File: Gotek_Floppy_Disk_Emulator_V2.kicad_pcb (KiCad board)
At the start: 2 copper layers, 90 x 60 mm, 66 parts, among them J1 Power Connector, J2 OLED Display 0.91" Module, J3 USB_A, J5 Programming Connector, J6 Floppy Data Connector, Q1 MMBT2222, Q2 BSS123, Q3 BSS123, Q4 BSS123, Q5 BSS123, Q6 BSS123, Q7 BSS123, SW1 KY040 Rotary Encoder Module, SW2 DIP Switch, U1 AMS1117-3.3, U2 STM32F105RBTx, U3 STMPS2141, U4 74HCT04, Y1 8MHz

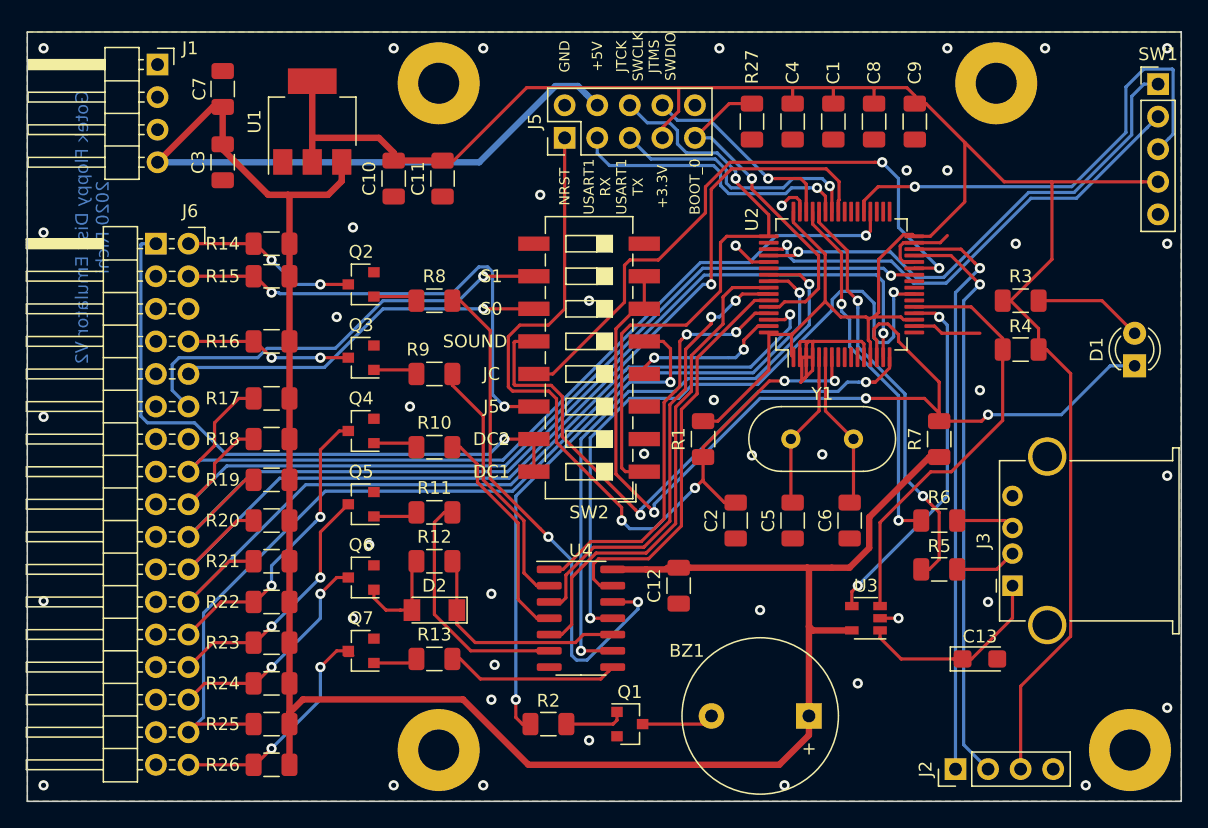
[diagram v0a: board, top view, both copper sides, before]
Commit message: Fixed PCB from original https://github.com/RichardRozehnal/Gotek-Floppy-Disk-Emulator-V2: * Add PCB edge cut for IDC 34-pin cable keying * Change Buzzer type from Active to Passive (single click on drive motor step) * Change "Buzzer_12x9.5RM7.6" footprint to "Buzzer_12x9.5RM6.5"
Update BoM.
Add Buzzer_12x9.5RM6.5 footprint and 3D model.
Delete unused files.
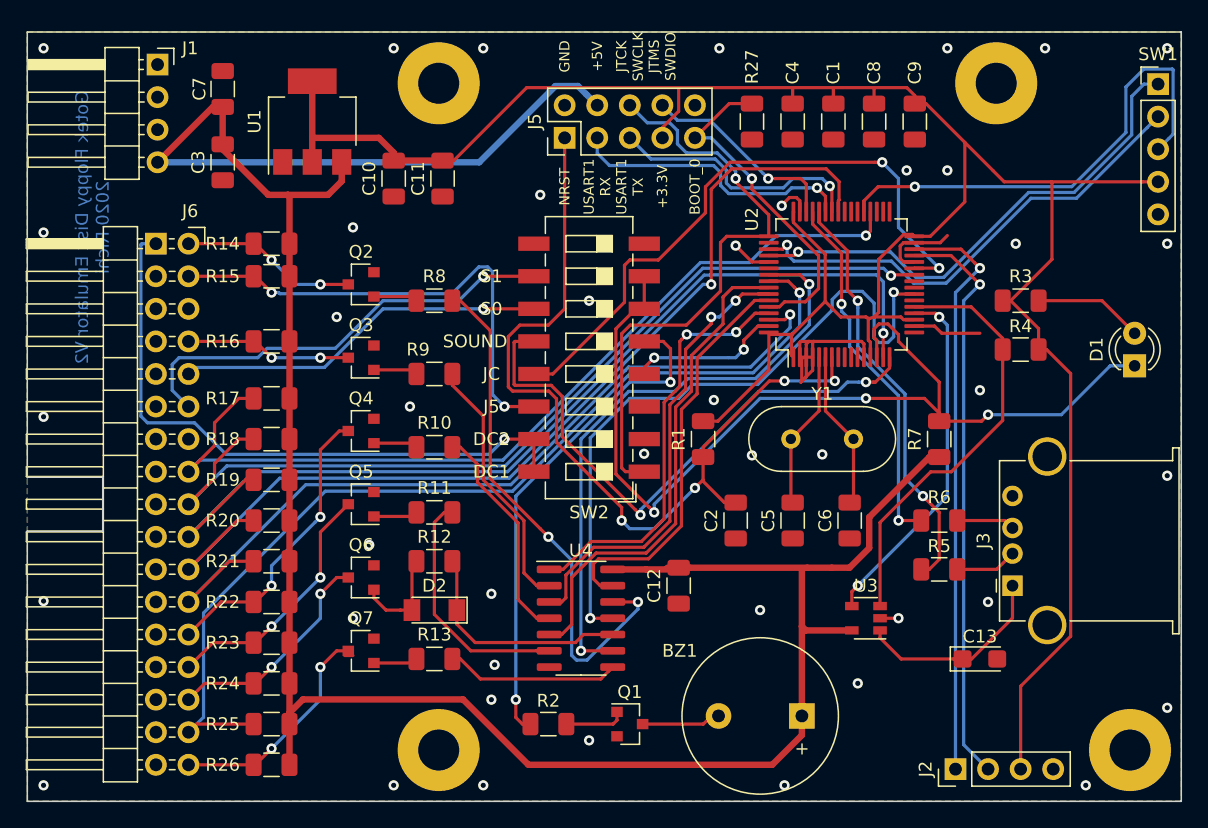
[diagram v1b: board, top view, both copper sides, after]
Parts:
- BZ1: value 5V Active Buzzer 12mm -> 5V Passive Buzzer 12mm; footprint Gotek_Floppy_Disk_Emulator_V2:Buzzer_12x9.5RM7.6 -> Gotek_Floppy_Disk_Emulator_V2:Buzzer_12x9.5RM6.5
- moved BZ1 0.55 mm to (142.3, 109.2)
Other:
- outline, holes or cut-outs redrawn
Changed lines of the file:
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@@
   (general
     (thickness 1.6)
-    (drawings 23)
-    (tracks 855)
+    (drawings 27)
+    (tracks 854)
     (zones 0)
     (modules 66)
@@
     (add_net +5V)
   )
+  (module Gotek_Floppy_Disk_Emulator_V2:Buzzer_12x9.5RM6.5 (layer F.Cu)
+    (at 142.325 109.22 180)
+    (descr "Generic Buzzer, D12mm height 9.5mm with RM6.5mm")
+    (tags buzzer)
+    (fp_text reference BZ1 (at 9.525 5.08) (layer F.SilkS)
+      (effects (font (size 1 1) (thickness 0.15)))
+    )
+    (fp_text value "5V Passive Buzzer 12mm" (at 3.8 7.4) (layer F.Fab)
+      (effects (font (size 1 1) (thickness 0.15)))
+    )
+    (fp_text user + (at -0.01 -2.54) (layer F.SilkS)
+      (effects (font (size 1 1) (thickness 0.15)))
+    )
+    (fp_text user + (at -0.01 -2.54) (layer F.SilkS)
+      (effects (font (size 1 1) (thickness 0.15)))
+    )
+    (fp_text user %R (at 3.8 -4) (layer F.Fab)
+      (effects (font (size 1 1) (thickness 0.15)))
+    )
+    (fp_circle (center 3.25 0) (end 9.5 0) (layer F.CrtYd) (width 0.05))
+    (fp_circle (center 3.25 0) (end 9.25 0) (layer F.Fab) (width 0.1))
+    (fp_circle (center 3.25 0) (end 4.25 0) (layer F.Fab) (width 0.1))
+    (fp_circle (center 3.25 0) (end 9.35 0) (layer F.SilkS) (width 0.12))
+    (pad 1 thru_hole rect (at 0 0 180) (size 2 2) (drill 1) (layers *.Cu *.Mask)
+      (net 2 +5V))
+    (pad 2 thru_hole circle (at 6.5 0 180) (size 2 2) (drill 1) (layers *.Cu *.Mask)
+      (net 1 "Net-(BZ1-Pad2)"))
+    (model ${KIPRJMOD}/libs/Gotek_Floppy_Disk_Emulator_V2.3dshapes/Buzzer_12x9.5RM6.5.wrl
+      (at (xyz 0 0 0))
+      (scale (xyz 1 1 1))
+      (rotate (xyz 0 0 0))
+    )
+  )
   (module Gotek_Floppy_Disk_Emulator_V2:LQFP-64_10x10mm_P0.5mm (layer F.Cu)
     (at 145.415 75.565 90)
@@
     )
   )
-  (module Gotek_Floppy_Disk_Emulator_V2:Buzzer_12x9.5RM7.6 (layer F.Cu)
-    (at 142.875 109.22 180)
-    (descr "Generic Buzzer, D12mm height 9.5mm with RM7.6mm")
-    (tags buzzer)
-    (fp_text reference BZ1 (at 9.525 5.08) (layer F.SilkS)
-      (effects (font (size 1 1) (thickness 0.15)))
-    )
-    (fp_text value "5V Active Buzzer 12mm" (at 3.8 7.4) (layer F.Fab)
-      (effects (font (size 1 1) (thickness 0.15)))
-    )
-    (fp_circle (center 3.8 0) (end 9.9 0) (layer F.SilkS) (width 0.12))
-    (fp_circle (center 3.8 0) (end 4.8 0) (layer F.Fab) (width 0.1))
-    (fp_circle (center 3.8 0) (end 9.8 0) (layer F.Fab) (width 0.1))
-    (fp_circle (center 3.8 0) (end 10.05 0) (layer F.CrtYd) (width 0.05))
-    (fp_text user %R (at 3.8 -4) (layer F.Fab)
-      (effects (font (size 1 1) (thickness 0.15)))
-    )
-    (fp_text user + (at -0.01 -2.54) (layer F.SilkS)
-      (effects (font (size 1 1) (thickness 0.15)))
-    )
-    (fp_text user + (at -0.01 -2.54) (layer F.Fab)
-      (effects (font (size 1 1) (thickness 0.15)))
-    )
-    (pad 2 thru_hole circle (at 7.6 0 180) (size 2 2) (drill 1) (layers *.Cu *.Mask)
-      (net 1 "Net-(BZ1-Pad2)"))
-    (pad 1 thru_hole rect (at 0 0 180) (size 2 2) (drill 1) (layers *.Cu *.Mask)
-      (net 2 +5V))
-    (model ${KISYS3DMOD}/Buzzer_Beeper.3dshapes/Buzzer_12x9.5RM7.6.wrl
-      (at (xyz 0 0 0))
-      (scale (xyz 1 1 1))
-      (rotate (xyz 0 0 0))
-    )
-  )
   (module Gotek_Floppy_Disk_Emulator_V2:C_1206_3216Metric (layer F.Cu)
     (at 144.78 62.865 270)
@@
     )
   )
+  (gr_line (start 87.8 90.6) (end 81.915 90.6) (layer Edge.Cuts) (width 0.12))
+  (gr_line (start 87.8 94.8) (end 87.8 90.6) (layer Edge.Cuts) (width 0.12))
+  (gr_line (start 81.915 94.8) (end 87.8 94.8) (layer Edge.Cuts) (width 0.12))
+  (gr_line (start 81.915 55.88) (end 81.915 90.6) (layer Edge.Cuts) (width 0.12))
   (dimension 60 (width 0.12) (layer Dwgs.User)
     (gr_text "60.000 mm" (at 185.42 85.88 270) (layer Dwgs.User)
@@
     (effects (font (size 0.8 0.8) (thickness 0.15)))
   )
-  (gr_line (start 81.915 115.88) (end 81.915 55.88) (layer Edge.Cuts) (width 0.12))
+  (gr_line (start 81.915 115.88) (end 81.915 94.8) (layer Edge.Cuts) (width 0.12))
   (gr_line (start 171.915 115.88) (end 81.915 115.88) (layer Edge.Cuts) (width 0.12))
   (gr_line (start 171.915 55.88) (end 171.915 115.88) (layer Edge.Cuts) (width 0.12))
@@
   (segment (start 147.57501 93.72499) (end 147.57501 96.1278) (width 0.5) (layer F.Cu) (net 2))
   (segment (start 147.57501 96.1278) (end 146.04281 97.66) (width 0.5) (layer F.Cu) (net 2))
-  (segment (start 142.875 110.72) (end 142.875 109.22) (width 0.5) (layer F.Cu) (net 2))
-  (segment (start 140.565 113.03) (end 142.875 110.72) (width 0.5) (layer F.Cu) (net 2))
+  (segment (start 142.325 110.72) (end 142.325 109.22) (width 0.5) (layer F.Cu) (net 2))
+  (segment (start 140.015 113.03) (end 142.325 110.72) (width 0.5) (layer F.Cu) (net 2))
   (segment (start 102.365 109.855) (end 102.365 108.98) (width 0.5) (layer F.Cu) (net 2))
   (segment (start 102.365 108.98) (end 103.415001 107.929999) (width 0.5) (layer F.Cu) (net 2))
   (segment (start 103.415001 107.929999) (end 115.896001 107.929999) (width 0.5) (layer F.Cu) (net 2))
   (segment (start 115.896001 107.929999) (end 120.996002 113.03) (width 0.5) (layer F.Cu) (net 2))
-  (segment (start 120.996002 113.03) (end 140.565 113.03) (width 0.5) (layer F.Cu) (net 2))
+  (segment (start 120.996002 113.03) (end 140.015 113.03) (width 0.5) (layer F.Cu) (net 2))
   (segment (start 146.04281 97.66) (end 144.65 97.66) (width 0.5) (layer F.Cu) (net 2))
   (segment (start 144.65 97.66) (end 142.745 97.66) (width 0.5) (layer F.Cu) (net 2))
-  (segment (start 142.745 97.66) (end 142.875 97.79) (width 0.5) (layer F.Cu) (net 2))
   (segment (start 142.745 97.66) (end 133.59 97.66) (width 0.5) (layer F.Cu) (net 2))
-  (segment (start 143.19 102.55) (end 146.22 102.55) (width 0.5) (layer F.Cu) (net 2))
-  (segment (start 142.875 102.235) (end 143.19 102.55) (width 0.5) (layer F.Cu) (net 2))
-  (segment (start 142.875 97.79) (end 142.875 102.235) (width 0.5) (layer F.Cu) (net 2))
-  (segment (start 142.875 102.235) (end 142.875 109.22) (width 0.5) (layer F.Cu) (net 2))
+  (segment (start 142.64 102.55) (end 146.22 102.55) (width 0.5) (layer F.Cu) (net 2))
+  (segment (start 142.325 102.235) (end 142.64 102.55) (width 0.5) (layer F.Cu) (net 2))
+  (segment (start 142.325 97.79) (end 142.325 102.235) (width 0.5) (layer F.Cu) (net 2))
+  (segment (start 142.325 102.235) (end 142.325 109.22) (width 0.5) (layer F.Cu) (net 2))
   (segment (start 96.39 61.725) (end 97.155 61.725) (width 0.5) (layer F.Cu) (net 2))
   (segment (start 92.075 66.04) (end 96.39 61.725) (width 0.5) (layer F.Cu) (net 2))
